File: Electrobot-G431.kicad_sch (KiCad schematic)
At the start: 1 part

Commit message: Mise à jour du schéma d'exemple
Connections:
- net +5V: now reaches A1.27 (+5V)
- net GND: now reaches A1.29 (GND)
- net GND: now also A1.4 (GND)
- no-connect marks 3 -> 6
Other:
- note added: "L'alimentation du module se fera en +5V Les entrées codeurs doivent être divisées pour convertir 5V -> 3.3V (le CPU ne supporte pas le 5V)"

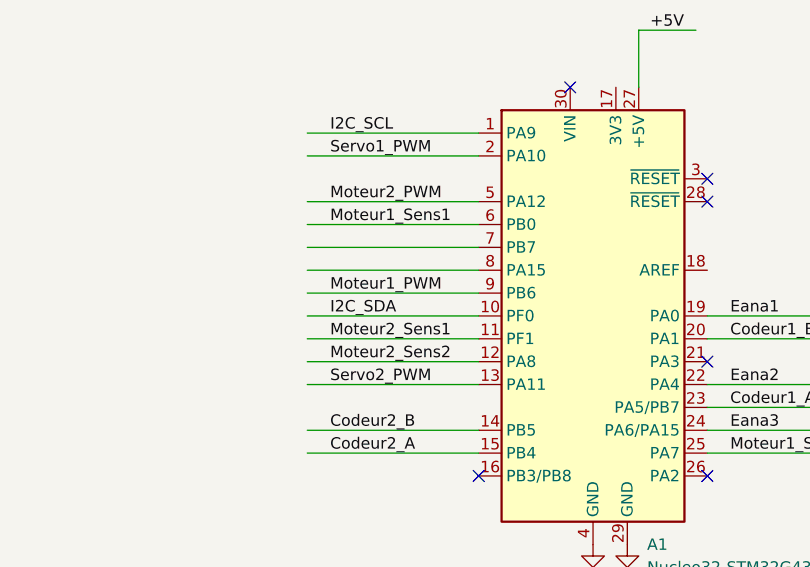
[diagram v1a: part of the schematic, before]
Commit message: Ajout d'1 entrée analogique + 1 sortie servomoteur
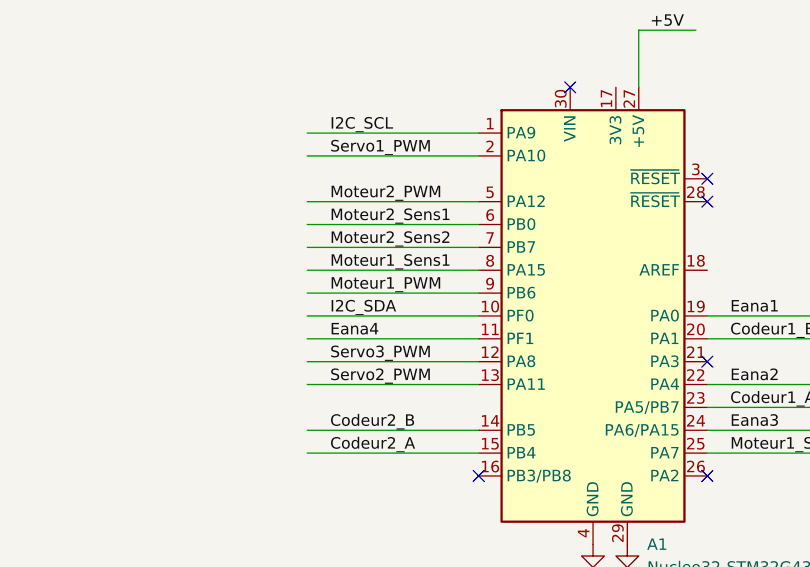
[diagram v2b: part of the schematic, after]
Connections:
- net Moteur1_Sens1: now also A1.8 (PA15); no longer A1.6 (PB0)
- net Moteur2_Sens1: now also A1.6 (PB0); no longer A1.11 (PF1)
- net Moteur2_Sens2: now also A1.7 (PB7); no longer A1.12 (PA8)
- new net Eana4: A1.11 (PF1)
- new net Servo3_PWM: A1.12 (PA8)
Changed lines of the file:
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@@
+		)
+	)
+	(label "Eana4"
+		(at 111.76 91.44 0)
+		(fields_autoplaced yes)
+		(effects
+			(font
+				(size 1.27 1.27)
+			)
+			(justify left bottom)
 		)
 	)
@@
 	)
 	(label "Moteur2_Sens2"
-		(at 111.76 93.98 0)
+		(at 111.76 81.28 0)
 		(fields_autoplaced yes)
 		(effects
@@
 		)
 	)
-	(label "Moteur2_Sens1"
-		(at 111.76 91.44 0)
+	(label "Moteur1_Sens1"
+		(at 111.76 83.82 0)
 		(fields_autoplaced yes)
 		(effects
@@
 		)
 	)
-	(label "Moteur1_Sens1"
+	(label "Moteur2_Sens1"
 		(at 111.76 78.74 0)
 		(fields_autoplaced yes)
 		(effects
+			(font
+				(size 1.27 1.27)
+			)
+			(justify left bottom)
+		)
+	)
+	(label "Servo3_PWM"
+		(at 111.76 93.98 0)
+		(fields_autoplaced yes)
+		(effects

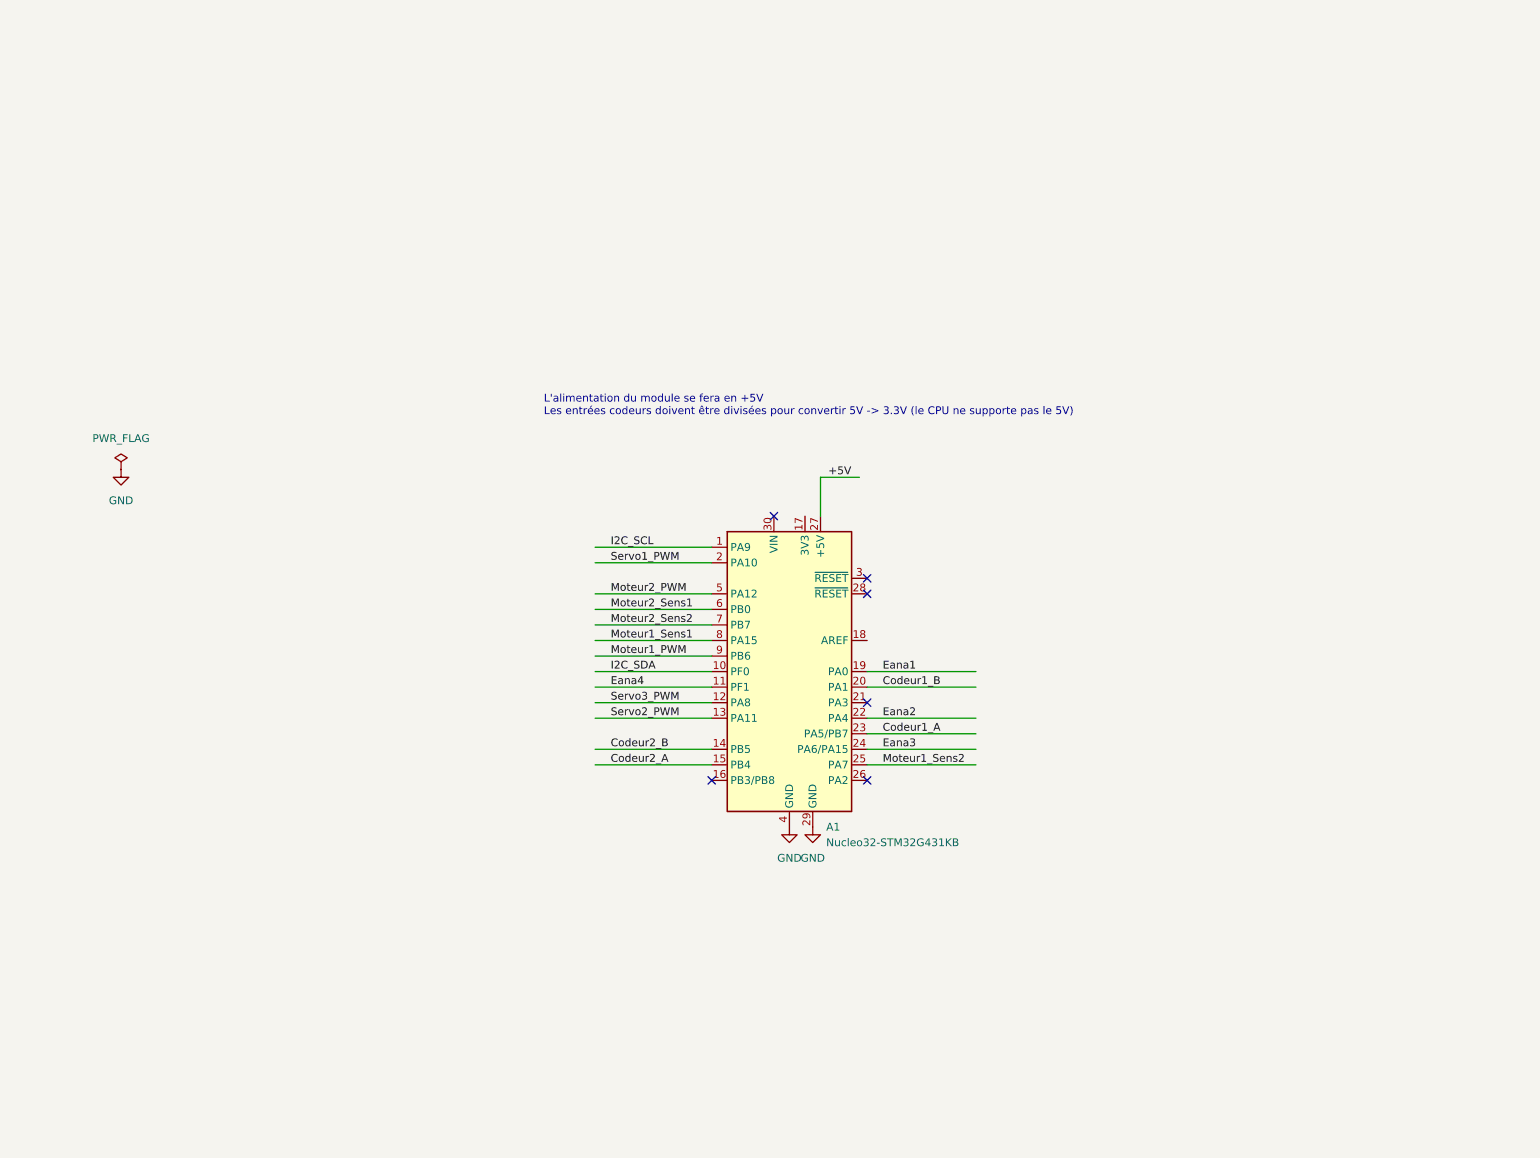
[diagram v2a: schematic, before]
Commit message: Mise à jour du schéma suite à séance CRLG du 13/01/2025
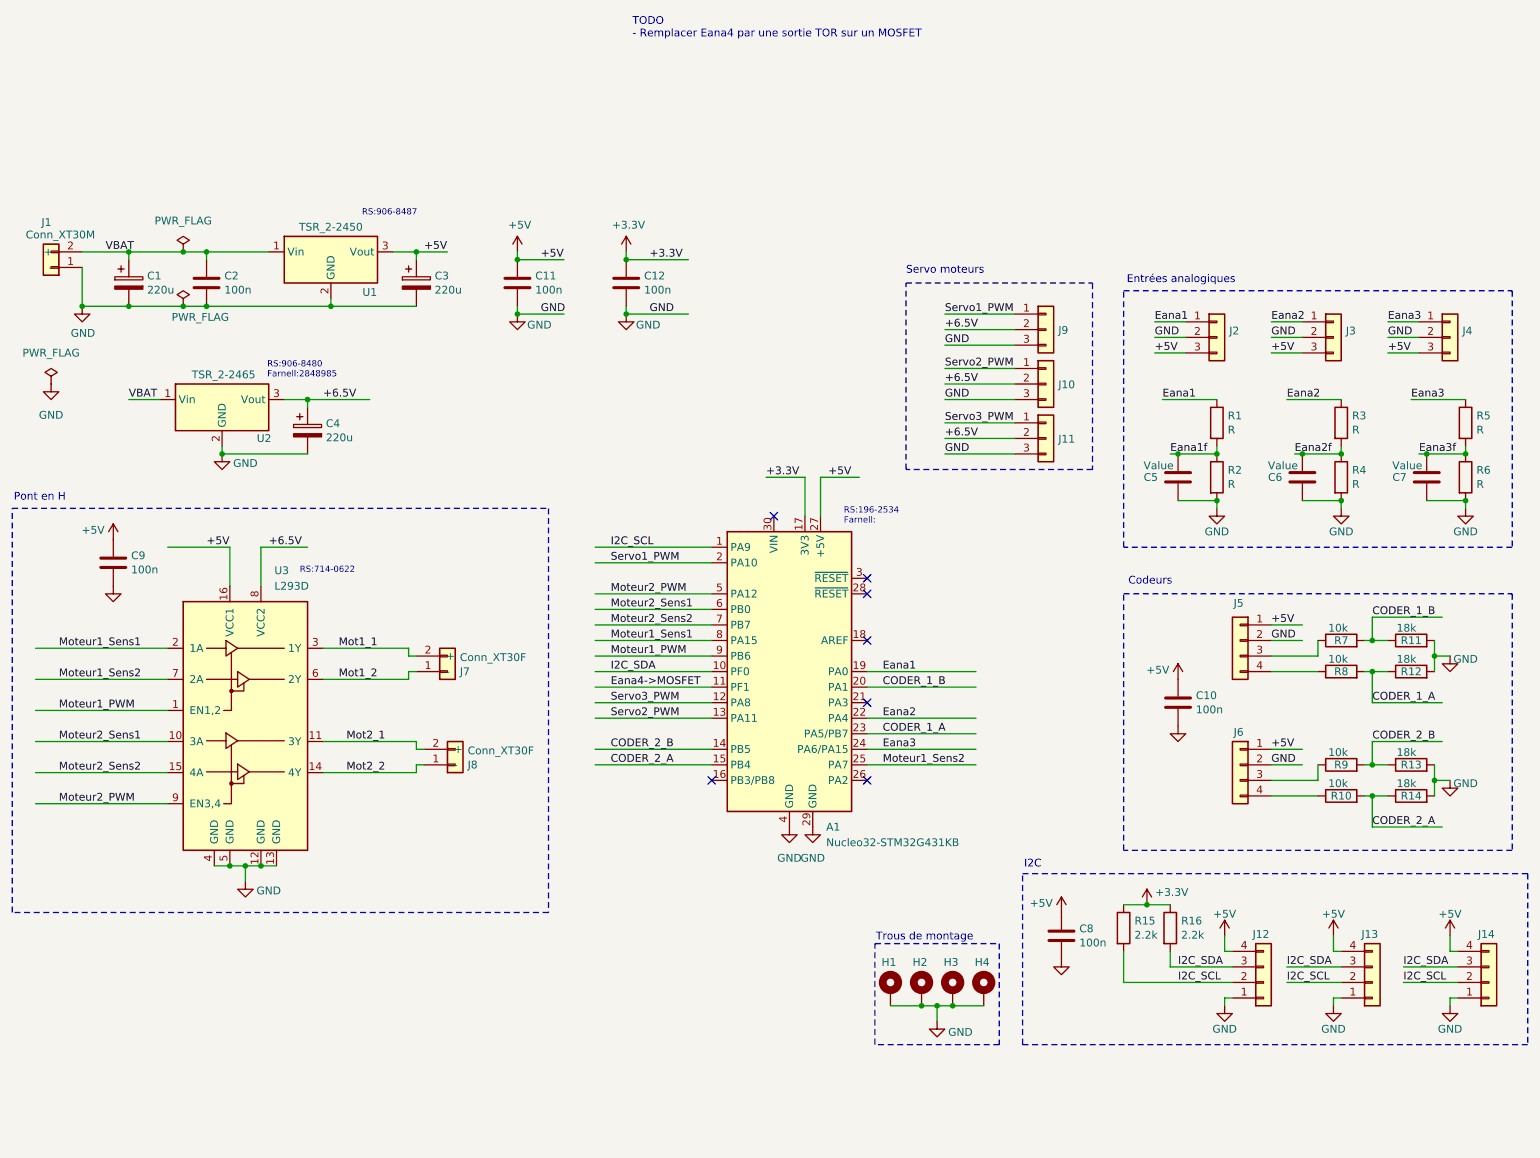
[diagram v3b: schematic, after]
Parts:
- added C1, C3, C4: 220u, Passive:C_Radial_D8.0mm_H11.5mm_P3.50mm, symbol CRLG-Passive:CP
- added C10, C11, C12, C2, C8, C9: 100n, Capacitor_SMD:C_1206_3216Metric, symbol CRLG-Passive:C
- added C5, C6, C7: Value, Capacitor_SMD:C_1206_3216Metric, symbol CRLG-Passive:C
- added H1, H2, H3, H4: MountingHole_Pad, MountingHole:MountingHole_3.2mm_M3_Pad, symbol Mechanical:MountingHole_Pad
- added J1: Conn_XT30M, XT30:AMASS_XT30UPB-M_1x02_P5.0mm_Vertical, symbol CRLG-Connectors:Conn_XT30M
- added J10, J11, J9: Conn_01x03, Servomotors:Servomotor-3x254, symbol CRLG-Connectors:Conn_01x03
- added J12, J13, J14, J5, J6: Conn_01x04, Connector_Molex:Molex_KK-254_AE-6410-04A_1x04_P2.54mm_Vertical, symbol CRLG-Connectors:Conn_01x04
- added J2, J3, J4: Conn_01x03, Connector_Molex:Molex_KK-254_AE-6410-03A_1x03_P2.54mm_Vertical, symbol CRLG-Connectors:Conn_01x03
- added J7, J8: Conn_XT30F, XT30:AMASS_XT30UPB-F_1x02_P5.0mm_Vertical, symbol CRLG-Connectors:Conn_XT30F
- added R1, R2, R3, R4, R5, R6: R, Resistor_SMD:R_1206_3216Metric, symbol CRLG-Passive:R
- added R10, R7, R8, R9: 10k, Resistor_SMD:R_1206_3216Metric, symbol CRLG-Passive:R
- added R11, R12, R13, R14: 18k, Resistor_SMD:R_1206_3216Metric, symbol CRLG-Passive:R
- added R15, R16: 2.2k, Resistor_SMD:R_1206_3216Metric, symbol CRLG-Passive:R
- added U1: TSR_2-2450, Converter_DCDC:Converter_DCDC_TRACO_TSR-1_THT, symbol CRLG_Regulators:TSR_2-2450
- added U2: TSR_2-2465, Converter_DCDC:Converter_DCDC_TRACO_TSR-1_THT, symbol CRLG_Regulators:TSR_2-2465
- added U3: L293D, Package_DIP:DIP-16_W7.62mm, symbol Driver_Motor:L293D
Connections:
- net +5V: now also C10.1, C11.1, C3.1, C8.1, C9.1, J12.4 (Pin_4), J13.4 (Pin_4), J14.4 (Pin_4), J2.3 (Pin_3), J3.3 (Pin_3), J4.3 (Pin_3), J5.1 (Pin_1), J6.1 (Pin_1), U1.3 (Vout), U3.16 (VCC1)
- net Eana1: now also J2.1 (Pin_1), R1.1
- net Eana2: now also J3.1 (Pin_1), R3.1
- net Eana3: now also J4.1 (Pin_1), R5.1
- net GND: now also C1.2, C10.2, C11.2, C12.2, C2.2, C3.2, C4.2, C5.1, C6.1, C7.1, C8.2, C9.2, H1.1, H2.1, H3.1, H4.1, J1.1 (-), J10.3 (Pin_3), J11.3 (Pin_3), J12.1 (Pin_1), J13.1 (Pin_1), J14.1 (Pin_1), J2.2 (Pin_2), J3.2 (Pin_2), J4.2 (Pin_2), J5.2 (Pin_2), J6.2 (Pin_2), J9.3 (Pin_3), R11.2, R12.2, R13.2, R14.2, R2.2, R4.2, R6.2, U1.2 (GND), U2.2 (GND), U3.12 (GND), U3.13 (GND), U3.4 (GND), U3.5 (GND)
- net I2C_SCL: now also J12.2 (Pin_2), J13.2 (Pin_2), J14.2 (Pin_2), R15.2
- net I2C_SDA: now also J12.3 (Pin_3), J13.3 (Pin_3), J14.3 (Pin_3), R16.2
- net Moteur1_PWM: now also U3.1 (EN1,2)
- net Moteur1_Sens1: now also U3.2 (1A)
- net Moteur1_Sens2: now also U3.7 (2A)
- net Moteur2_PWM: now also U3.9 (EN3,4)
- net Moteur2_Sens1: now also U3.10 (3A)
- net Moteur2_Sens2: now also U3.15 (4A)
- net Servo1_PWM: now also J9.1 (Pin_1)
- net Servo2_PWM: now also J10.1 (Pin_1)
- net Servo3_PWM: now also J11.1 (Pin_1)
- net +3.3V: now reaches A1.17 (3V3)
- net +3.3V: now also C12.1, R15.1, R16.1
- net Codeur1_A renamed CODER_1_A
- net CODER_1_A: now also R12.1, R8.2
- net Codeur1_B renamed CODER_1_B
- net CODER_1_B: now also R11.1, R7.2
- net Codeur2_A renamed CODER_2_A
- net CODER_2_A: now also R10.2, R14.1
- net Codeur2_B renamed CODER_2_B
- net CODER_2_B: now also R13.1, R9.2
- net Eana4 renamed Eana4->MOSFET
- new net: J6.3 (Pin_3), R9.1
- new net: J6.4 (Pin_4), R10.1
- new net: J5.3 (Pin_3), R7.1
- new net: J5.4 (Pin_4), R8.1
- new net +6.5V: C4.1, J10.2 (Pin_2), J11.2 (Pin_2), J9.2 (Pin_2), U2.3 (Vout), U3.8 (VCC2)
- new net Eana1f: C5.2, R1.2, R2.1
- new net Eana2f: C6.2, R3.2, R4.1
- new net Eana3f: C7.2, R5.2, R6.1
- new net Mot1_1: J7.2 (+), U3.3 (1Y)
- new net Mot1_2: J7.1 (-), U3.6 (2Y)
- new net Mot2_1: J8.2 (+), U3.11 (3Y)
- new net Mot2_2: J8.1 (-), U3.14 (4Y)
- new net VBAT: C1.1, C2.1, J1.2 (+), U1.1 (Vin), U2.1 (Vin)
- no-connect marks 6 -> 7
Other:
- note added: "Codeurs"
- note added: "Entrées analogiques"
- note added: "I2C"
- note added: "Pont en H"
- note added: "RS:196-2534 Farnell:"
- note added: "RS:714-0622"
- note added: "RS:906-8480 Farnell:2848985"
- note added: "RS:906-8487"
- note added: "Servo moteurs"
- note added: "TODO - Remplacer Eana4 par une sortie TOR sur un MOSFET"
- note added: "Trous de montage"
- note removed: "L'alimentation du module se fera en +5V Les entrées codeurs doivent être divisées pour convertir 5V -> 3.3V (le CPU ne supporte pas le 5V)"

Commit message: Ajout du MOSFET BSP-76 en remplacement de Eana4
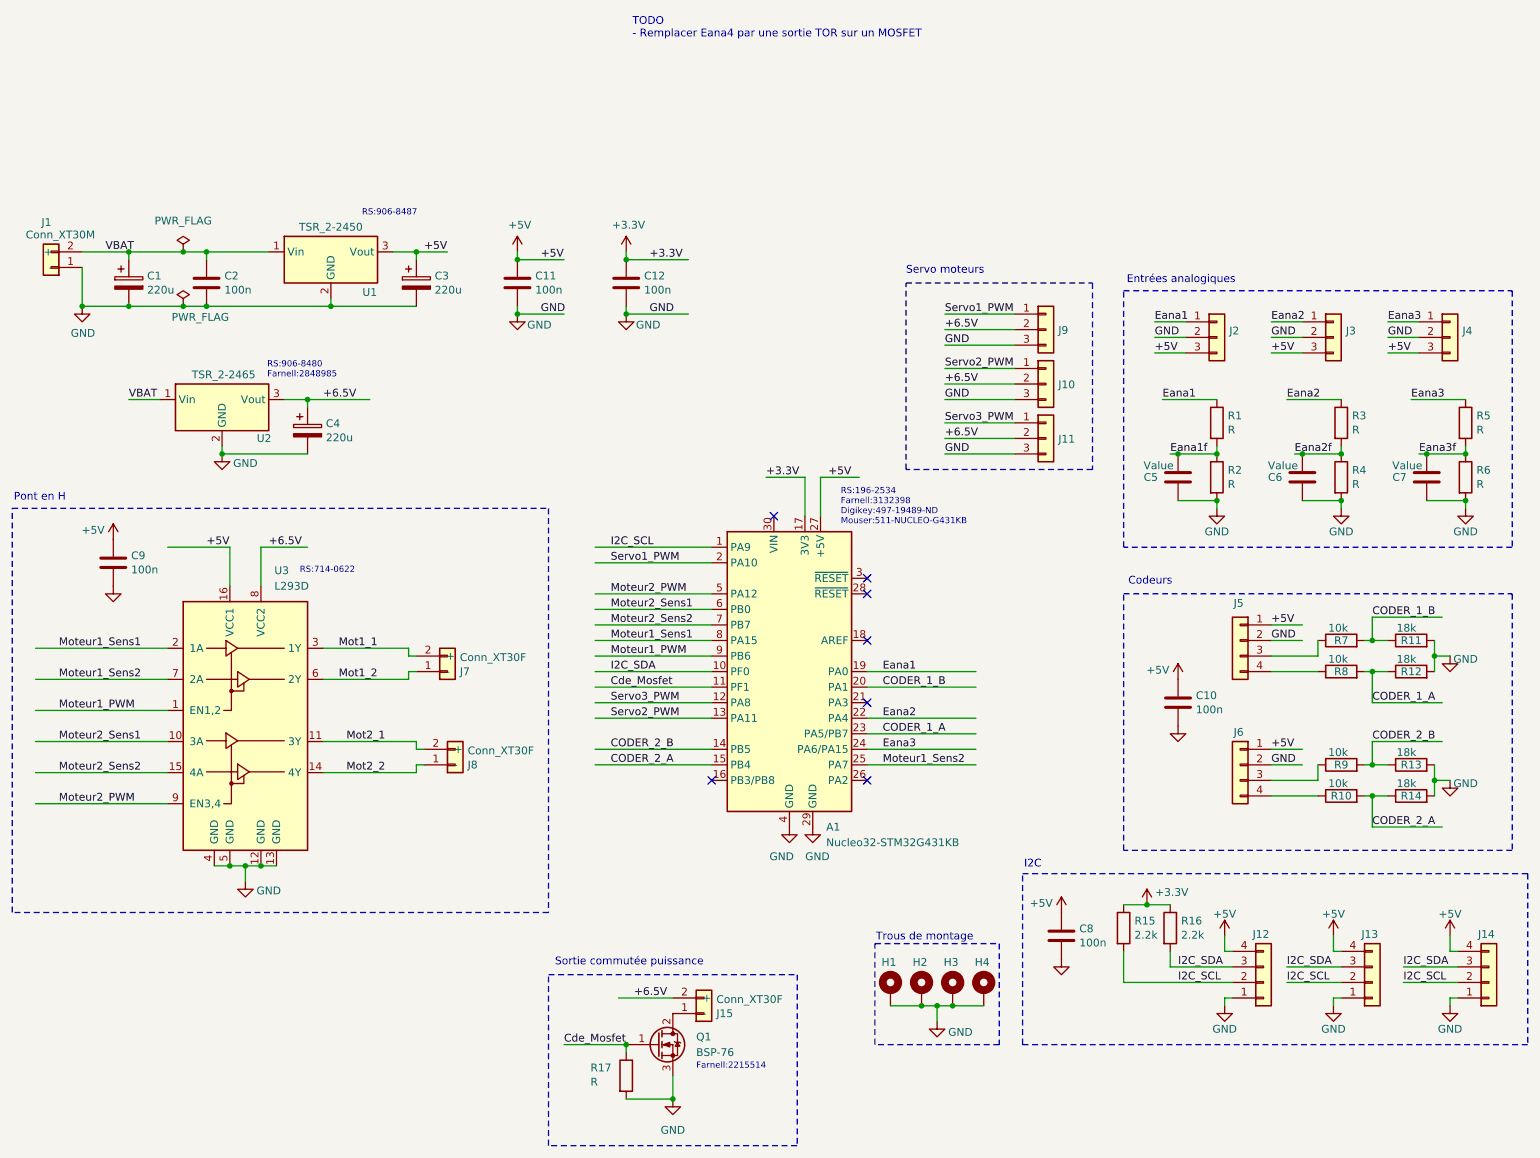
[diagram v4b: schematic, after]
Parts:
- added J15: Conn_XT30F, XT30:AMASS_XT30UPB-F_1x02_P5.0mm_Vertical, symbol CRLG-Connectors:Conn_XT30F
- added Q1: BSP-76, Package_TO_SOT_SMD:SOT-223-3_TabPin2, symbol CRLG_Transistors:BSP-76
- added R17: R, Resistor_SMD:R_1206_3216Metric, symbol CRLG-Passive:R
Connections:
- net +6.5V: now also J15.2 (+)
- net GND: now also Q1.3 (S), R17.2
- net Eana4->MOSFET renamed Cde_Mosfet
- net Cde_Mosfet: now also Q1.1 (G), R17.1
- new net: J15.1 (-), Q1.2 (D)
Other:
- note added: "Farnell:2215514"
- note added: "RS:196-2534 Farnell:3132398 Digikey:497-19489-ND Mouser:511-NUCLEO-G431KB"
- note added: "Sortie commutée puissance"
- note removed: "RS:196-2534 Farnell:"
